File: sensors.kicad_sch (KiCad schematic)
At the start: 3 parts, among them U6 BMI055

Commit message: Update placement
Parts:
- C19, C20: footprint Capacitor_SMD:C_0603_1608Metric -> Capacitor_SMD:C_0402_1005Metric
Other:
- moved on the sheet: C19, C20, U6

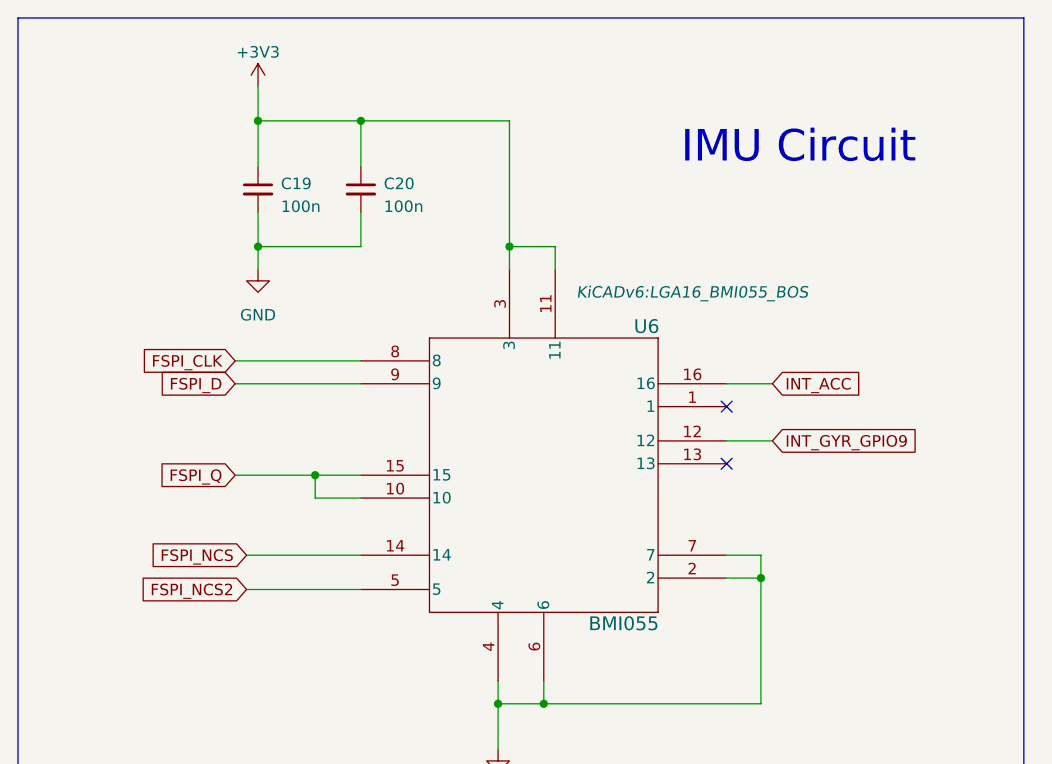
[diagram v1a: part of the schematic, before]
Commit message: route usb and flash
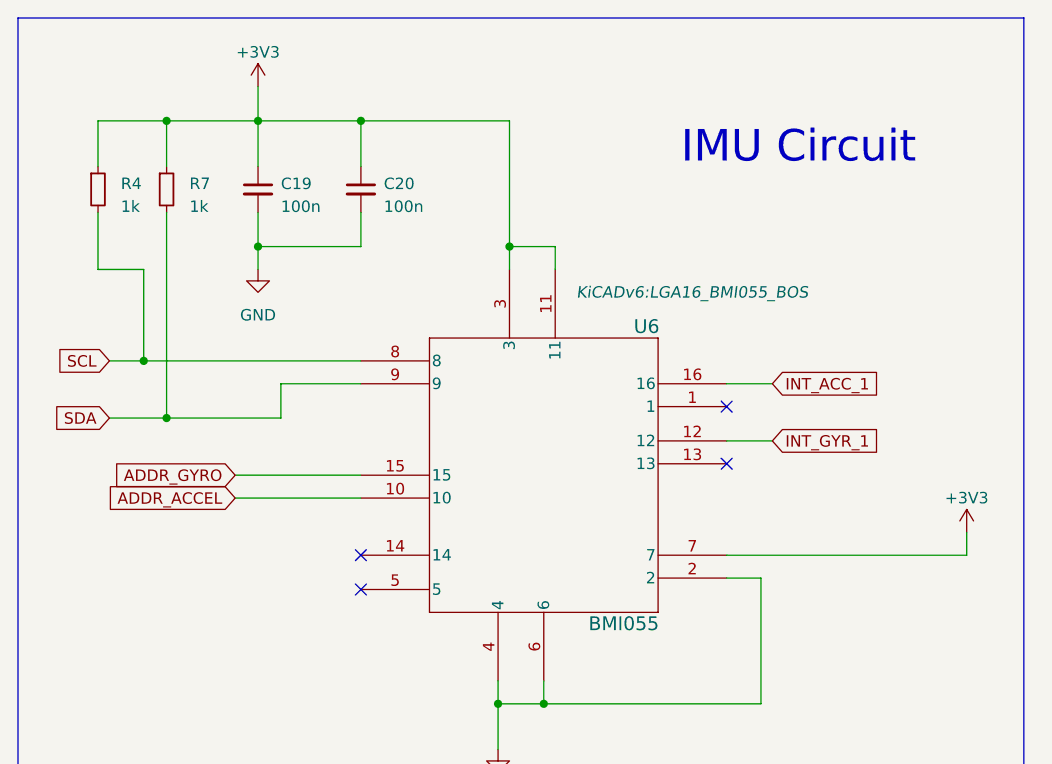
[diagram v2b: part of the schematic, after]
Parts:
- added R4, R7: 1k, Resistor_SMD:R_0402_1005Metric, symbol Device:R_Small
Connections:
- net +3V3: now also U6.7, R4.1, R7.1
- net GND: no longer U6.7
- net FSPI_CLK renamed SCL
- net SCL: now also R4.2
- net FSPI_D renamed SDA
- net SDA: now also R7.2
- net FSPI_NCS: no longer names the net of U6.14
- net FSPI_NCS2: no longer names the net of U6.5
- net FSPI_Q renamed ADDR_ACCEL
- net ADDR_ACCEL: no longer U6.15
- net INT_ACC renamed INT_ACC_1
- net INT_GYR_GPIO9 renamed INT_GYR_1
- new net ADDR_GYRO: U6.15
- no-connect marks 2 -> 4
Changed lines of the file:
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@@
   (junction (at 107.95 54.61) (diameter 0) (color 0 0 0 0)
   )
-  (junction (at 86.36 80.01) (diameter 0) (color 0 0 0 0)
+  (junction (at 69.85 73.66) (diameter 0) (color 0 0 0 0)
+  )
+  (junction (at 67.31 67.31) (diameter 0) (color 0 0 0 0)
+  )
+  (junction (at 69.85 40.64) (diameter 0) (color 0 0 0 0)
   )
   (junction (at 111.76 105.41) (diameter 0) (color 0 0 0 0)
@@
   (junction (at 80.01 40.64) (diameter 0) (color 0 0 0 0)
   )
-  (junction (at 135.89 91.44) (diameter 0) (color 0 0 0 0)
-  )
   (junction (at 80.01 54.61) (diameter 0) (color 0 0 0 0)
   )
+  (no_connect (at 91.44 92.71))
   (no_connect (at 132.08 78.74))
+  (no_connect (at 91.44 88.9))
   (no_connect (at 132.08 72.39))
-  (wire (pts (xy 91.44 92.71) (xy 78.74 92.71))
+  (wire (pts (xy 69.85 50.8) (xy 69.85 73.66))
     (stroke (width 0) (type default))
   )
@@
     (stroke (width 0) (type default))
   )
-  (wire (pts (xy 91.44 82.55) (xy 86.36 82.55))
+  (wire (pts (xy 77.47 82.55) (xy 91.44 82.55))
     (stroke (width 0) (type default))
   )
@@
     (stroke (width 0) (type default))
   )
-  (wire (pts (xy 86.36 80.01) (xy 86.36 82.55))
+  (wire (pts (xy 67.31 67.31) (xy 91.44 67.31))
+    (stroke (width 0) (type default))
+  )
+  (wire (pts (xy 82.55 73.66) (xy 82.55 69.85))
     (stroke (width 0) (type default))
   )
@@
     (stroke (width 0) (type default))
   )
-  (wire (pts (xy 86.36 80.01) (xy 77.47 80.01))
+  (wire (pts (xy 67.31 57.15) (xy 67.31 67.31))
     (stroke (width 0) (type default))
   )
@@
     (stroke (width 0) (type default))
   )
+  (wire (pts (xy 69.85 73.66) (xy 82.55 73.66))
+    (stroke (width 0) (type default))
+  )
+  (wire (pts (xy 62.23 40.64) (xy 69.85 40.64))
+    (stroke (width 0) (type default))
+  )
   (wire (pts (xy 107.95 54.61) (xy 107.95 57.15))
     (stroke (width 0) (type default))
@@
     (stroke (width 0) (type default))
   )
-  (wire (pts (xy 132.08 88.9) (xy 135.89 88.9))
+  (wire (pts (xy 158.75 86.36) (xy 158.75 88.9))
+    (stroke (width 0) (type default))
+  )
+  (wire (pts (xy 132.08 88.9) (xy 158.75 88.9))
     (stroke (width 0) (type default))
   )
@@
     (stroke (width 0) (type default))
   )
-  (wire (pts (xy 77.47 67.31) (xy 91.44 67.31))
+  (wire (pts (xy 82.55 69.85) (xy 91.44 69.85))
+    (stroke (width 0) (type default))
+  )
+  (wire (pts (xy 63.5 67.31) (xy 67.31 67.31))
     (stroke (width 0) (type default))
   )
@@
     (stroke (width 0) (type default))
   )
-  (wire (pts (xy 91.44 88.9) (xy 78.74 88.9))
-    (stroke (width 0) (type default))
-  )
   (wire (pts (xy 80.01 40.64) (xy 91.44 40.64))
     (stroke (width 0) (type default))
   )
+  (wire (pts (xy 69.85 45.72) (xy 69.85 40.64))
+    (stroke (width 0) (type default))
+  )
+  (wire (pts (xy 62.23 57.15) (xy 67.31 57.15))
+    (stroke (width 0) (type default))
+  )
   (wire (pts (xy 80.01 40.64) (xy 80.01 45.72))
     (stroke (width 0) (type default))
@@
     (stroke (width 0) (type default))
   )
-  (wire (pts (xy 91.44 80.01) (xy 86.36 80.01))
+  (wire (pts (xy 77.47 80.01) (xy 91.44 80.01))
     (stroke (width 0) (type default))
   )
@@
     (stroke (width 0) (type default))
   )
+  (wire (pts (xy 62.23 45.72) (xy 62.23 40.64))
+    (stroke (width 0) (type default))
+  )
   (wire (pts (xy 107.95 40.64) (xy 107.95 54.61))
     (stroke (width 0) (type default))
   )
-  (wire (pts (xy 77.47 69.85) (xy 91.44 69.85))
+  (wire (pts (xy 63.5 73.66) (xy 69.85 73.66))
+    (stroke (width 0) (type default))
+  )
+  (wire (pts (xy 69.85 40.64) (xy 80.01 40.64))
     (stroke (width 0) (type default))
   )
@@
     (stroke (width 0) (type default))
   )
+  (wire (pts (xy 62.23 50.8) (xy 62.23 57.15))
+    (stroke (width 0) (type default))
+  )
   (wire (pts (xy 132.08 91.44) (xy 135.89 91.44))
-    (stroke (width 0) (type default))
-  )
-  (wire (pts (xy 135.89 88.9) (xy 135.89 91.44))
     (stroke (width 0) (type default))
   )
@@
     (effects (font (size 3.5 3.5)) (justify left bottom))
   )
-  (global_label "INT_GYR_GPIO9" (shape input) (at 137.16 76.2 0) (fields_autoplaced)
+  (global_label "INT_GYR_1" (shape input) (at 137.16 76.2 0) (fields_autoplaced)
     (effects (font (size 1.27 1.27)) (justify left))
-    (property "Intersheetrefs" "${INTERSHEET_REFS}" (at 154.2173 76.2 0)
+    (property "Intersheetrefs" "${INTERSHEET_REFS}" (at 149.742 76.2 0)
       (effects (font (size 1.27 1.27)) (justify left) hide)
     )
   )
-  (global_label "FSPI_NCS" (shape input) (at 78.74 88.9 180) (fields_autoplaced)
+  (global_label "SDA" (shape input) (at 63.5 73.66 180) (fields_autoplaced)
     (effects (font (size 1.27 1.27)) (justify right))
-    (property "Intersheetrefs" "${INTERSHEET_REFS}" (at 66.8837 88.9 0)
+    (property "Intersheetrefs" "${INTERSHEET_REFS}" (at 57.0261 73.66 0)
       (effects (font (size 1.27 1.27)) (justify right) hide)
     )
   )
-  (global_label "FSPI_D" (shape input) (at 77.47 69.85 180) (fields_autoplaced)
+  (global_label "SCL" (shape input) (at 63.5 67.31 180) (fields_autoplaced)
     (effects (font (size 1.27 1.27)) (justify right))
-    (property "Intersheetrefs" "${INTERSHEET_REFS}" (at 68.1537 69.85 0)
+    (property "Intersheetrefs" "${INTERSHEET_REFS}" (at 57.0866 67.31 0)
       (effects (font (size 1.27 1.27)) (justify right) hide)
     )
   )
-  (global_label "FSPI_CLK" (shape input) (at 77.47 67.31 180) (fields_autoplaced)
+  (global_label "ADDR_ACCEL" (shape input) (at 77.47 82.55 180) (fields_autoplaced)
     (effects (font (size 1.27 1.27)) (justify right))
-    (property "Intersheetrefs" "${INTERSHEET_REFS}" (at 65.8556 67.31 0)
+    (property "Intersheetrefs" "${INTERSHEET_REFS}" (at 62.8923 82.55 0)
       (effects (font (size 1.27 1.27)) (justify right) hide)
     )
   )
-  (global_label "FSPI_Q" (shape input) (at 77.47 80.01 180) (fields_autoplaced)
+  (global_label "ADDR_GYRO" (shape input) (at 77.47 80.01 180) (fields_autoplaced)
     (effects (font (size 1.27 1.27)) (justify right))
-    (property "Intersheetrefs" "${INTERSHEET_REFS}" (at 68.0932 80.01 0)
+    (property "Intersheetrefs" "${INTERSHEET_REFS}" (at 63.7389 80.01 0)
       (effects (font (size 1.27 1.27)) (justify right) hide)
     )
   )
-  (global_label "INT_ACC" (shape input) (at 137.16 69.85 0) (fields_autoplaced)
+  (global_label "INT_ACC_1" (shape input) (at 137.16 69.85 0) (fields_autoplaced)
     (effects (font (size 1.27 1.27)) (justify left))
-    (property "Intersheetrefs" "${INTERSHEET_REFS}" (at 147.5649 69.85 0)
+    (property "Intersheetrefs" "${INTERSHEET_REFS}" (at 149.742 69.85 0)
       (effects (font (size 1.27 1.27)) (justify left) hide)
-    )
-  )
-  (global_label "FSPI_NCS2" (shape input) (at 78.74 92.71 180) (fields_autoplaced)
-    (effects (font (size 1.27 1.27)) (justify right))
-    (property "Intersheetrefs" "${INTERSHEET_REFS}" (at 65.6742 92.71 0)
-      (effects (font (size 1.27 1.27)) (justify right) hide)
     )
   )
@@
     )
   )
+  (symbol (lib_id "Device:R_Small") (at 62.23 48.26 0) (unit 1)
+    (in_bom yes) (on_board yes) (dnp no) (fields_autoplaced)
+    (property "Reference" "R4" (at 64.77 47.625 0)
+      (effects (font (size 1.27 1.27)) (justify left))
+    )
+    (property "Value" "1k" (at 64.77 50.165 0)
+      (effects (font (size 1.27 1.27)) (justify left))
+    )
+    (property "Footprint" "Resistor_SMD:R_0402_1005Metric" (at 62.23 48.26 0)
+      (effects (font (size 1.27 1.27)) hide)
+    )
+    (property "Datasheet" "~" (at 62.23 48.26 0)
+      (effects (font (size 1.27 1.27)) hide)
+    )
+    (pin "1")
+    (pin "2")
+    (instances
+      (project "RC-Car-Controller"
+        (path "/6532ed18-dd14-44a4-a4f8-6383f8135b66/7627e0c1-a993-485b-b38b-14ad3d8f424c"
+          (reference "R4") (unit 1)
+        )
+      )
+    )
+  )
   (symbol (lib_id "power:GND") (at 80.01 57.15 0) (unit 1)
     (in_bom yes) (on_board yes) (dnp no) (fields_autoplaced)
@@
     )
   )
+  (symbol (lib_id "power:+3V3") (at 158.75 86.36 0) (unit 1)
+    (in_bom yes) (on_board yes) (dnp no) (fields_autoplaced)
+    (property "Reference" "#PWR022" (at 158.75 90.17 0)
+      (effects (font (size 1.27 1.27)) hide)
+    )
+    (property "Value" "+3V3" (at 158.75 82.55 0)
+      (effects (font (size 1.27 1.27)))
+    )
+    (property "Footprint" "" (at 158.75 86.36 0)
+      (effects (font (size 1.27 1.27)) hide)
+    )
+    (property "Datasheet" "" (at 158.75 86.36 0)
+      (effects (font (size 1.27 1.27)) hide)
+    )
+    (pin "1")
+    (instances
+      (project "RC-Car-Controller"
+        (path "/6532ed18-dd14-44a4-a4f8-6383f8135b66"
+          (reference "#PWR022") (unit 1)
+        )
+        (path "/6532ed18-dd14-44a4-a4f8-6383f8135b66/7627e0c1-a993-485b-b38b-14ad3d8f424c"
+          (reference "#PWR020") (unit 1)
+        )
+      )
+    )
+  )
   (symbol (lib_id "Device:C_Small") (at 80.01 48.26 0) (unit 1)
     (in_bom yes) (on_board yes) (dnp no) (fields_autoplaced)
@@
         )
       )
+    )
+  )
+  (symbol (lib_id "Device:R_Small") (at 69.85 48.26 0) (unit 1)
+    (in_bom yes) (on_board yes) (dnp no) (fields_autoplaced)
+    (property "Reference" "R7" (at 72.39 47.625 0)
+      (effects (font (size 1.27 1.27)) (justify left))
+    )
+    (property "Value" "1k" (at 72.39 50.165 0)
+      (effects (font (size 1.27 1.27)) (justify left))
+    )
+    (property "Footprint" "Resistor_SMD:R_0402_1005Metric" (at 69.85 48.26 0)
+      (effects (font (size 1.27 1.27)) hide)
+    )
+    (property "Datasheet" "~" (at 69.85 48.26 0)
+      (effects (font (size 1.27 1.27)) hide)
+    )
+    (pin "1")
+    (pin "2")
+    (instances
+      (project "RC-Car-Controller"
+        (path "/6532ed18-dd14-44a4-a4f8-6383f8135b66/7627e0c1-a993-485b-b38b-14ad3d8f424c"
+          (reference "R7") (unit 1)
+        )
+      )

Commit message: route motors
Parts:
- renumbered C20 to C10, C19 to C9, U6 to U4
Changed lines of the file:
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@@
   (symbol (lib_id "BMI055:BMI055") (at 91.44 72.39 0) (unit 1)
     (in_bom yes) (on_board yes) (dnp no)
-    (property "Reference" "U6" (at 123.19 63.5 0)
+    (property "Reference" "U4" (at 123.19 63.5 0)
       (effects (font (size 1.524 1.524)))
     )
@@
     (instances
       (project "RC-Car-Controller"
-        (path "/6532ed18-dd14-44a4-a4f8-6383f8135b66"
-          (reference "U6") (unit 1)
-        )
         (path "/6532ed18-dd14-44a4-a4f8-6383f8135b66/7627e0c1-a993-485b-b38b-14ad3d8f424c"
           (reference "U4") (unit 1)
@@
   (symbol (lib_id "power:GND") (at 106.68 110.49 0) (unit 1)
     (in_bom yes) (on_board yes) (dnp no) (fields_autoplaced)
-    (property "Reference" "#PWR023" (at 106.68 116.84 0)
+    (property "Reference" "#PWR019" (at 106.68 116.84 0)
       (effects (font (size 1.27 1.27)) hide)
     )
@@
     (instances
       (project "RC-Car-Controller"
-        (path "/6532ed18-dd14-44a4-a4f8-6383f8135b66"
-          (reference "#PWR023") (unit 1)
-        )
         (path "/6532ed18-dd14-44a4-a4f8-6383f8135b66/7627e0c1-a993-485b-b38b-14ad3d8f424c"
           (reference "#PWR019") (unit 1)
@@
   (symbol (lib_id "power:+3V3") (at 80.01 36.83 0) (unit 1)
     (in_bom yes) (on_board yes) (dnp no) (fields_autoplaced)
-    (property "Reference" "#PWR022" (at 80.01 40.64 0)
+    (property "Reference" "#PWR017" (at 80.01 40.64 0)
       (effects (font (size 1.27 1.27)) hide)
     )
@@
     (instances
       (project "RC-Car-Controller"
-        (path "/6532ed18-dd14-44a4-a4f8-6383f8135b66"
-          (reference "#PWR022") (unit 1)
-        )
         (path "/6532ed18-dd14-44a4-a4f8-6383f8135b66/7627e0c1-a993-485b-b38b-14ad3d8f424c"
           (reference "#PWR017") (unit 1)
@@
   (symbol (lib_id "power:GND") (at 80.01 57.15 0) (unit 1)
     (in_bom yes) (on_board yes) (dnp no) (fields_autoplaced)
-    (property "Reference" "#PWR021" (at 80.01 63.5 0)
+    (property "Reference" "#PWR018" (at 80.01 63.5 0)
       (effects (font (size 1.27 1.27)) hide)
     )
@@
     (instances
       (project "RC-Car-Controller"
-        (path "/6532ed18-dd14-44a4-a4f8-6383f8135b66"
-          (reference "#PWR021") (unit 1)
-        )
         (path "/6532ed18-dd14-44a4-a4f8-6383f8135b66/7627e0c1-a993-485b-b38b-14ad3d8f424c"
           (reference "#PWR018") (unit 1)
@@
   (symbol (lib_id "power:+3V3") (at 158.75 86.36 0) (unit 1)
     (in_bom yes) (on_board yes) (dnp no) (fields_autoplaced)
-    (property "Reference" "#PWR022" (at 158.75 90.17 0)
+    (property "Reference" "#PWR020" (at 158.75 90.17 0)
       (effects (font (size 1.27 1.27)) hide)
     )
@@
     (instances
       (project "RC-Car-Controller"
-        (path "/6532ed18-dd14-44a4-a4f8-6383f8135b66"
-          (reference "#PWR022") (unit 1)
-        )
         (path "/6532ed18-dd14-44a4-a4f8-6383f8135b66/7627e0c1-a993-485b-b38b-14ad3d8f424c"
           (reference "#PWR020") (unit 1)
@@
   (symbol (lib_id "Device:C_Small") (at 80.01 48.26 0) (unit 1)
     (in_bom yes) (on_board yes) (dnp no) (fields_autoplaced)
-    (property "Reference" "C19" (at 82.55 47.6313 0)
+    (property "Reference" "C9" (at 82.55 47.6313 0)
       (effects (font (size 1.27 1.27)) (justify left))
     )
@@
     (instances
       (project "RC-Car-Controller"
-        (path "/6532ed18-dd14-44a4-a4f8-6383f8135b66"
-          (reference "C19") (unit 1)
-        )
         (path "/6532ed18-dd14-44a4-a4f8-6383f8135b66/7627e0c1-a993-485b-b38b-14ad3d8f424c"
           (reference "C9") (unit 1)
@@
   (symbol (lib_id "Device:C_Small") (at 91.44 48.26 0) (unit 1)
     (in_bom yes) (on_board yes) (dnp no) (fields_autoplaced)
-    (property "Reference" "C20" (at 93.98 47.6313 0)
+    (property "Reference" "C10" (at 93.98 47.6313 0)
       (effects (font (size 1.27 1.27)) (justify left))
     )
@@
     (instances
       (project "RC-Car-Controller"
-        (path "/6532ed18-dd14-44a4-a4f8-6383f8135b66"
-          (reference "C20") (unit 1)
-        )
         (path "/6532ed18-dd14-44a4-a4f8-6383f8135b66/7627e0c1-a993-485b-b38b-14ad3d8f424c"
           (reference "C10") (unit 1)
